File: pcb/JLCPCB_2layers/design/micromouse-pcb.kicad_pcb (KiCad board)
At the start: 4 copper layers, 100 x 120 mm, 184 parts, among them J1 BATT_IN_2S, J10 BATT_IN_XT60 (parallel option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, J5 MOTOR_A_N20_ENCODER, J6 MOTOR_B_N20_ENCODER, J7 USB-C rear (GCT USB4105; VBUS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, J8 JTAG_1x6 (3V3,TMS,TCK,TDO,TDI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, J9 BALANCE_2S, Q1 Q_PMOS reverse guard (DMP3098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, Q16 BSS138 (real part; Q_NMOS_GSD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, Q17 BSS138 (real part; Q_NMOS_GSD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, Q18 BSS138 (real part; Q_NMOS_GSD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, Q19 BSS138 (real part; Q_NMOS_GSD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, Q2 PT334-6B (5mm filtered PT; LO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, Q20 BSS138 (real part; Q_NMOS_GSD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, Q21 BSS138 (real part; Q_NMOS_GSD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, Q22 BSS138 (real part; Q_NMOS_GSD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, Q23 BSS138 (real part; Q_NMOS_GSD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, Q24 BSS138 (real part; Q_NMOS_GSD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, Q25 BSS138 (real part; Q_NMOS_GSD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, Q26 BSS138 (real part; Q_NMOS_GSD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, Q27 BSS138 (real part; Q_NMOS_GSD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, Q28 BSS84 (PMOS indicator driver;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, Q29 BSS84 (PMOS indicator driver;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, Q3 PT334-6B (5mm filtered PT; LO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, Q30 BSS84 (PMOS indicator driver;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, Q31 BSS84 (PMOS indicator driver;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, Q32 BSS84 (PMOS indicator driver;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, Q33 BSS84 (PMOS indicator driver;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, Q34 MMBT2222A (buzzer low-side dr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, Q4 PT334-6B (5mm filtered PT; LO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, Q5 PT334-6B (5mm filtered PT; LO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, Q6 PT334-6B (5mm filtered PT; LO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, Q7 PT334-6B (5mm filtered PT; LO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, SW1 BTN_A (start / BOOT), SW2 RESET, SW3 BTN_B, SW4 BTN_C, SW5 PWR ALL (PCM12SMTR slide; sli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, SW6 PWR MOTORS (PCM12SMTR slide; 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, U1 AP63203WU-7 (fixed 3.3V 2A bu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, U2 TB6612FNG, U3 ESP32-S3-WROOM-1-N8R2 (quad P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, U4 CD74HC4067M, U6 USBLC6-2SC6 (SOT-23-6; 2P6 ba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, U7 TPS54302DDCR (6.0V/3A motor b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, U8 BNO055 (9-axis IMU + fusion; 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

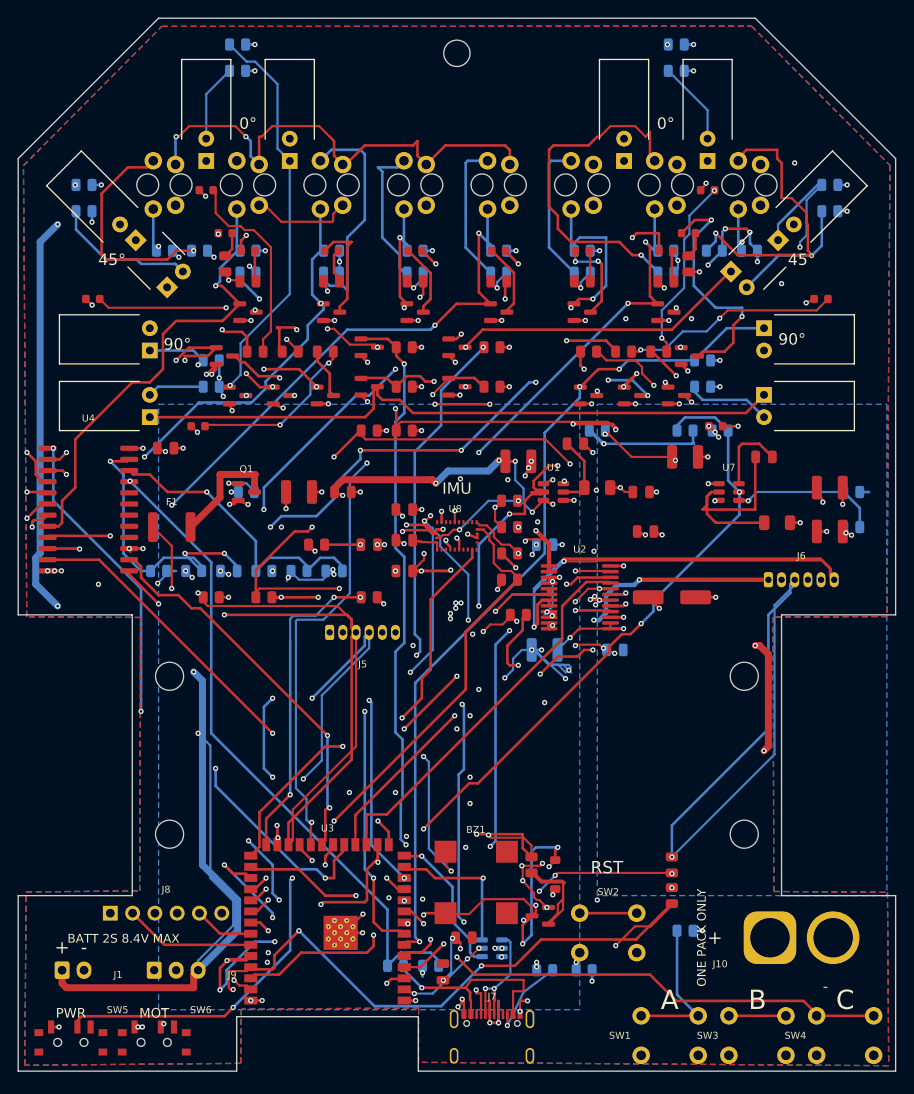
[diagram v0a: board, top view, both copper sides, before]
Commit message: 2-layer JLCPCB: initial placement + render (for review)
build_pcb.py adapted for the 2-layer part set:
- 2 copper layers (was 4); inner GND/3V3 planes replaced by solid GND pours on
  both outer layers (power rails routed as traces in the routing phase).
- Skip-missing placement wrapper drops the removed parts (line array LS1-8,
  line indicators, mux U4, JTAG J8) automatically; retained parts keep their
  4-layer positions.
- Restored the buzzer cluster (BZ1/Q34/D29/R81) + XT60 J10 placements (they were
  hand-placed in the frozen 4-layer board, never in build_pcb.py).
- Placed the new power/status/RGB LEDs (D30/D31/D32 + R82/R83/C31), provisional.
- THT hand-solder-margin gate downgraded to advisory (board is JLC machine-
  assembled); the one flagged pair (SW2<->R12, 2.04mm) will be nudged clear in
  refinement.

Board: 2 layers, 137 footprints, all 398 pins mapped, no courtyard overlaps,
bodies inside outline. Renders in images/placement_{top,bottom}.png.

Refinement next: motor connectors J5/J6 symmetric, J9 balance "OPTIONAL" silk,
confirm side indicators clear of IR beams, ALL refdes on silk, route to DRC 0/0.

Co-Authored-By: Claude Fable 5 <noreply@anthropic.com>
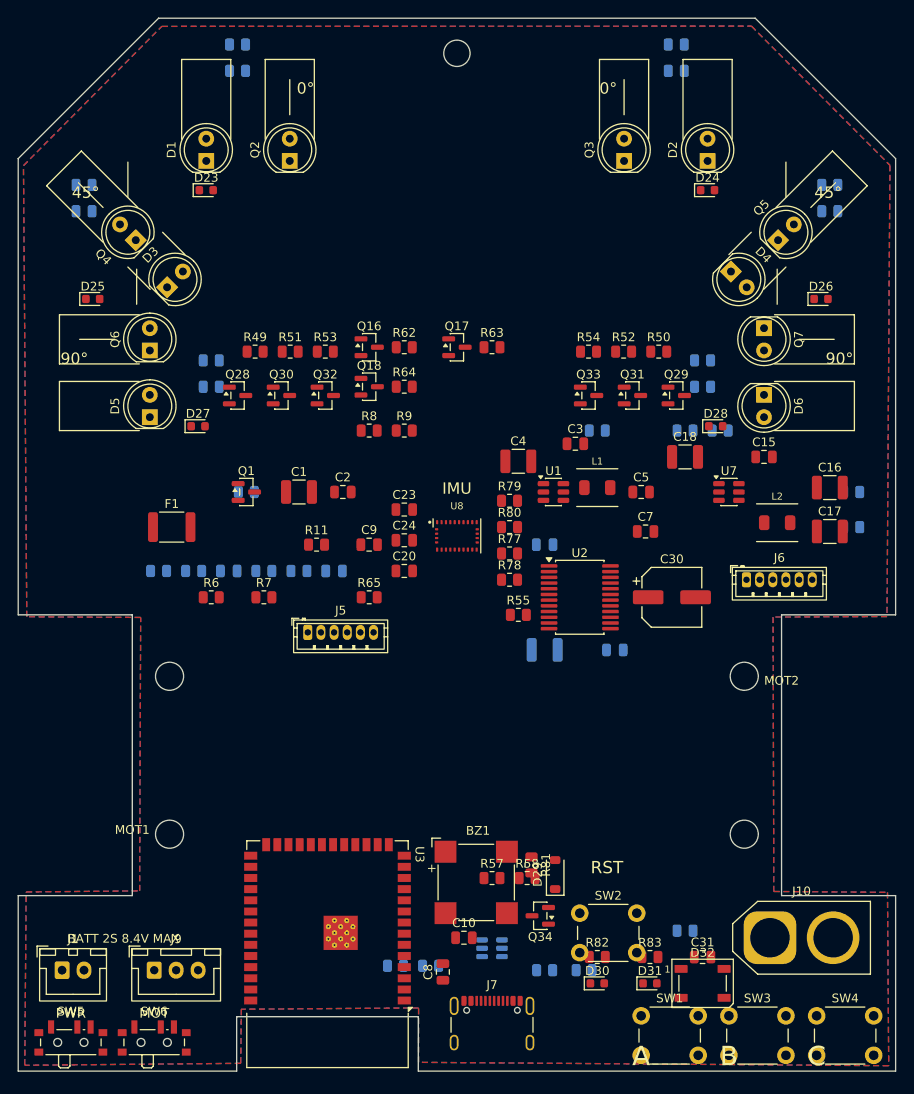
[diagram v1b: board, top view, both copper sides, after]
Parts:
- removed C13: 100nF, Capacitor_SMD:C_0805_2012Metric
- removed D15, D16, D17, D18, D19, D20, D21, D22: Indicator LED 0603 super-red AlInGaP, high-efficiency bin R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, LED_SMD:LED_0603_1608Metric
- removed J8: JTAG_1x6 (3V3,TMS,TCK,TDO,TDI,GND), Connector_PinHeader_2.54mm:PinHeader_1x06_P2.54mm_Vertical
- removed LS1, LS2, LS3, LS4, LS5, LS6, LS7, LS8: TCRT5000 (reflective sensor, filtered PT; PC817 base symbol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, n20:TCRT5000
- removed Q19, Q20, Q21, Q22, Q23, Q24, Q25, Q26, Q27: BSS138 (real part; Q_NMOS_GSD base symbol used so ERC check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, Package_TO_SOT_SMD:SOT-23
- removed R25, R27, R29, R31, R33, R35, R37, R39: 47k, Resistor_SMD:R_0805_2012Metric
- removed R26, R28, R30, R32, R34, R36, R38, R40: 120, Resistor_SMD:R_0805_2012Metric
- removed R41, R42, R43, R44, R45, R46, R47, R48: 1k, Resistor_SMD:R_0805_2012Metric
- removed R61: 100k, Resistor_SMD:R_0805_2012Metric
- removed U4: CD74HC4067M, Package_SO:SOIC-24W_7.5x15.4mm_P1.27mm
- added C31: C_0805_2012Metric, C_0805_2012Metric, F.Cu at (78.0, 107.0)
- added D30: LED_0603_1608Metric, LED_0603_1608Metric, F.Cu at (66.0, 110.0)
- added D31: LED_0603_1608Metric, LED_0603_1608Metric, F.Cu at (72.0, 110.0)
- added D32: LED_WS2812B_PLCC4_5.0x5.0mm_P3.2mm, LED_WS2812B_PLCC4_5.0x5.0mm_P3.2mm, F.Cu at (78.0, 110.0)
- added R82: R_0805_2012Metric, R_0805_2012Metric, F.Cu at (66.0, 107.0)
- added R83: R_0805_2012Metric, R_0805_2012Metric, F.Cu at (72.0, 107.0)
- BZ1: value CMT-8504-100-SMT (magnetic transducer 8.5mm, 15R coil, 4kHz; pads 3/4 are mechanical dummies) -> MagneticBuzzer_CUI_CMT-8504-100-SMT; footprint Buzzer_Beeper:MagneticBuzzer_CUI_CMT-8504-100-SMT -> MagneticBuzzer_CUI_CMT-8504-100-SMT
- C1, C11, C16, C17, C18, C4: footprint Capacitor_SMD:C_1210_3225Metric -> C_1210_3225Metric
- C10: value 10uF -> C_0805_2012Metric; footprint Capacitor_SMD:C_0805_2012Metric -> C_0805_2012Metric
- C12, C14, C15, C2, C24, C3, C5, C7: footprint Capacitor_SMD:C_0805_2012Metric -> C_0805_2012Metric
- C19, C20, C23, C6, C8: value 100nF -> C_0805_2012Metric; footprint Capacitor_SMD:C_0805_2012Metric -> C_0805_2012Metric
- C30: footprint Capacitor_SMD:CP_Elec_6.3x7.7 -> CP_Elec_6.3x7.7
- C9: value 1uF -> C_0805_2012Metric; footprint Capacitor_SMD:C_0805_2012Metric -> C_0805_2012Metric
- D1, D2, D3, D4, D5, D6: value IR333-A (Everlight 5mm 940nm 20deg; LD271 base symbol; TSAL6400 is lifecycle-Obsolete at Lion) -> LED_D5.0mm_IRGrey; footprint LED_THT:LED_D5.0mm_IRGrey -> LED_D5.0mm_IRGrey
- D23, D24, D25, D26, D27, D28: value Indicator LED 0603 super-red AlInGaP, high-eff bin (e.g. APT1608SURCK) -> LED_0603_1608Metric; footprint LED_SMD:LED_0603_1608Metric -> LED_0603_1608Metric
- D29: value 1N4148W (flyback clamp across the buzzer coil) -> D_SOD-123; footprint Diode_SMD:D_SOD-123 -> D_SOD-123
- F1: value 2.6A/16V PPTC -> Fuse_1812_4532Metric; footprint Fuse:Fuse_1812_4532Metric -> Fuse_1812_4532Metric
- J1: value BATT_IN_2S -> JST_XH_B2B-XH-A_1x02_P2.50mm_Vertical; footprint Connector_JST:JST_XH_B2B-XH-A_1x02_P2.50mm_Vertical -> JST_XH_B2B-XH-A_1x02_P2.50mm_Vertical
- J10: value BATT_IN_XT60 (parallel option -- ONE PACK ONLY) -> AMASS_XT60-M_1x02_P7.20mm_Vertical; footprint Connector_AMASS:AMASS_XT60-M_1x02_P7.20mm_Vertical -> AMASS_XT60-M_1x02_P7.20mm_Vertical
- J5: value MOTOR_A_N20_ENCODER -> JST_ZH_B6B-ZR_1x06_P1.50mm_Vertical; footprint Connector_JST:JST_ZH_B6B-ZR_1x06_P1.50mm_Vertical -> JST_ZH_B6B-ZR_1x06_P1.50mm_Vertical
- J6: value MOTOR_B_N20_ENCODER -> JST_ZH_B6B-ZR_1x06_P1.50mm_Vertical; footprint Connector_JST:JST_ZH_B6B-ZR_1x06_P1.50mm_Vertical -> JST_ZH_B6B-ZR_1x06_P1.50mm_Vertical
- J7: value USB-C rear (GCT USB4105; VBUS unused -- battery powers the board) -> USB_C_Receptacle_GCT_USB4105-xx-A_16P_TopMnt_Horizontal; footprint Connector_USB:USB_C_Receptacle_GCT_USB4105-xx-A_16P_TopMnt_Horizontal -> USB_C_Receptacle_GCT_USB4105-xx-A_16P_TopMnt_Horizontal
- J9: value BALANCE_2S -> JST_XH_B3B-XH-A_1x03_P2.50mm_Vertical; footprint Connector_JST:JST_XH_B3B-XH-A_1x03_P2.50mm_Vertical -> JST_XH_B3B-XH-A_1x03_P2.50mm_Vertical
- L1, L2: footprint n20:L_Bourns_SRP4020TA -> L_Bourns_SRP4020TA
- Q1: value Q_PMOS reverse guard (DMP3098L-7: Vgs +/-20V, 2S-safe) -> SOT-23; footprint Package_TO_SOT_SMD:SOT-23 -> SOT-23
- Q16, Q17, Q18: value BSS138 (real part; Q_NMOS_GSD base symbol used so ERC checks pins) -> SOT-23; footprint Package_TO_SOT_SMD:SOT-23 -> SOT-23
- Q2, Q3, Q4, Q5, Q6, Q7: value PT334-6B (5mm filtered PT; LONG LEAD = EMITTER; SFH309 base symbol so ERC checks pins) -> LED_D5.0mm_IRBlack; footprint LED_THT:LED_D5.0mm_IRBlack -> LED_D5.0mm_IRBlack
- Q28, Q29, Q30, Q31, Q32, Q33: value BSS84 (PMOS indicator driver; Q_PMOS base symbol) -> SOT-23; footprint Package_TO_SOT_SMD:SOT-23 -> SOT-23
- Q34: value MMBT2222A (buzzer low-side driver; Q_NPN_BEC base symbol so ERC checks pins) -> SOT-23; footprint Package_TO_SOT_SMD:SOT-23 -> SOT-23
- R1, R2, R62, R63, R64, R69, R73, R75, R76: value 100k -> R_0805_2012Metric; footprint Resistor_SMD:R_0805_2012Metric -> R_0805_2012Metric
- R10, R11, R55, R6, R65, R67, R7, R79, R8, R80, R9: value 10k -> R_0805_2012Metric; footprint Resistor_SMD:R_0805_2012Metric -> R_0805_2012Metric
- R12, R56: value 5.1k -> R_0805_2012Metric; footprint Resistor_SMD:R_0805_2012Metric -> R_0805_2012Metric
- R13, R15, R17, R19, R21, R23: value 47k -> R_0805_2012Metric; footprint Resistor_SMD:R_0805_2012Metric -> R_0805_2012Metric
- R14, R16, R18, R20, R22, R24: value 33 -> R_0805_2012Metric; footprint Resistor_SMD:R_0805_2012Metric -> R_0805_2012Metric
- R3: value 39k -> R_0805_2012Metric; footprint Resistor_SMD:R_0805_2012Metric -> R_0805_2012Metric
- R49, R50, R51, R52, R53, R54, R57, R58: value 1k -> R_0805_2012Metric; footprint Resistor_SMD:R_0805_2012Metric -> R_0805_2012Metric
- R68: value 15k -> R_0805_2012Metric; footprint Resistor_SMD:R_0805_2012Metric -> R_0805_2012Metric
- R70: value 220k -> R_0805_2012Metric; footprint Resistor_SMD:R_0805_2012Metric -> R_0805_2012Metric
- R71: value 110k -> R_0805_2012Metric; footprint Resistor_SMD:R_0805_2012Metric -> R_0805_2012Metric
- R74: value 11k -> R_0805_2012Metric; footprint Resistor_SMD:R_0805_2012Metric -> R_0805_2012Metric
- R77, R78: value 4.7k -> R_0805_2012Metric; footprint Resistor_SMD:R_0805_2012Metric -> R_0805_2012Metric
- R81: value 220 -> R_0805_2012Metric; footprint Resistor_SMD:R_0805_2012Metric -> R_0805_2012Metric
- SW1: value BTN_A (start / BOOT) -> SW_PUSH_6mm; footprint Button_Switch_THT:SW_PUSH_6mm -> SW_PUSH_6mm
- SW2: value RESET -> SW_PUSH_6mm; footprint Button_Switch_THT:SW_PUSH_6mm -> SW_PUSH_6mm
- SW3: value BTN_B -> SW_PUSH_6mm; footprint Button_Switch_THT:SW_PUSH_6mm -> SW_PUSH_6mm
- SW4: value BTN_C -> SW_PUSH_6mm; footprint Button_Switch_THT:SW_PUSH_6mm -> SW_PUSH_6mm
- SW5: value PWR ALL (PCM12SMTR slide; slide-to-GND = OFF) -> SW_SPDT_PCM12; footprint Button_Switch_SMD:SW_SPDT_PCM12 -> SW_SPDT_PCM12
- SW6: value PWR MOTORS (PCM12SMTR slide; slide-to-GND = motors OFF) -> SW_SPDT_PCM12; footprint Button_Switch_SMD:SW_SPDT_PCM12 -> SW_SPDT_PCM12
- U1: value AP63203WU-7 (fixed 3.3V 2A buck; AP63200WU base symbol so ERC checks pins) -> TSOT-23-6; footprint Package_TO_SOT_SMD:TSOT-23-6 -> TSOT-23-6
- U2: value TB6612FNG -> SSOP-24_5.3x8.2mm_P0.65mm; footprint Package_SO:SSOP-24_5.3x8.2mm_P0.65mm -> SSOP-24_5.3x8.2mm_P0.65mm
- U3: value ESP32-S3-WROOM-1-N8R2 (quad PSRAM: IO35-37 usable; octal -R8 would lose them) -> ESP32-S3-WROOM-1; footprint RF_Module:ESP32-S3-WROOM-1 -> ESP32-S3-WROOM-1
- U6: value USBLC6-2SC6 (SOT-23-6; 2P6 base symbol so ERC checks pins) -> SOT-23-6; footprint Package_TO_SOT_SMD:SOT-23-6 -> SOT-23-6
- U7: value TPS54302DDCR (6.0V/3A motor buck; FB=100k/11k) -> SOT-23-6; footprint Package_TO_SOT_SMD:SOT-23-6 -> SOT-23-6
- U8: value BNO055 (9-axis IMU + fusion; 3.3V native; I2C 0x28) -> VAL; footprint n20:BNO055 -> BNO055
- moved R57 20.6 mm to (54.0, 98.0), turned to 0 degrees
- moved R58 16.6 mm to (58.0, 98.0), turned to 0 degrees
- moved J5 2.50 mm to (33.0, 70.0)
- moved J6 2.50 mm to (83.0, 64.0)
- moved J7 1.50 mm to (54.0, 115.7)
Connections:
- U3 pad 12: MUX_S3 -> BAT_MID_SENSE
- U3 pad 17: AIN1 -> VBUS_SENSE
- U3 pad 19: MUX_S0 -> AIN1
- U3 pad 20: MUX_S1 -> STATUS_LED
- U3 pad 21: MUX_S2 -> unconnected-(U3-IO13-Pad21)
- U3 pad 22: LINE_EMIT -> RGB_DATA
- U3 pad 32: JTAG_TCK -> unconnected-(U3-IO39-Pad32)
- U3 pad 33: JTAG_TDO -> unconnected-(U3-IO40-Pad33)
- U3 pad 34: JTAG_TDI -> unconnected-(U3-IO41-Pad34)
- U3 pad 35: JTAG_TMS -> unconnected-(U3-IO42-Pad35)
- U3 pad 7: MUX_SENSE -> VBAT_SENSE
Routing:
- net BATT_RAW: track 364.0 -> 0.00 mm, vias 8 -> 0
- net ENC2_A_S3: track 290.2 -> 0.00 mm, vias 15 -> 0
- net PLUS3V3: track 245.9 -> 0.00 mm, vias 79 -> 0
- net GND: track 235.8 -> 0.00 mm, vias 112 -> 0
- net ENC2_A: track 215.1 -> 0.00 mm, vias 7 -> 0
- net ENC2_B: track 200.2 -> 0.00 mm, vias 6 -> 0
- net WALL4_SENSE: track 157.1 -> 0.00 mm, vias 4 -> 0
- net WALL2_SENSE: track 139.5 -> 0.00 mm, vias 5 -> 0
- net PWR_EN: track 128.4 -> 0.00 mm, vias 6 -> 0
- net EMIT_LINE_K: track 128.4 -> 0.00 mm, vias 3 -> 0
- net ENC2_B_S3: track 120.1 -> 0.00 mm, vias 4 -> 0
- net WALL1_SENSE: track 117.0 -> 0.00 mm, vias 2 -> 0
- net MOT_EN: track 110.4 -> 0.00 mm, vias 5 -> 0
- net ESP_EN: track 107.2 -> 0.00 mm, vias 4 -> 0
- net ENC1_B: track 103.9 -> 0.00 mm, vias 8 -> 0
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- removed copper zone on In1.Cu, net GND
- removed copper zone on In2.Cu, net PLUS3V3
- removed copper zone on B.Cu, net VM_6V
- removed copper zone on B.Cu, net VM_BATT
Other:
- copper layers 4 -> 2
- board text removed: "+"
- board text removed: "-"
- board text removed: "ONE PACK ONLY"

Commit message: 2-layer placement refinement (user render feedback)
- Removed the U-shaped body-silk "boxes" around the wall-sensor LEDs; kept the
  0/45/90-deg angle callouts.
- Motor connectors J5/J6 now SYMMETRIC (both x=33/67, y=70) -- moved the motor
  driver U2 (+ C11/C12/C30) to the motor-bay center so J6's mirror spot is free.
- Moved the 3 user buttons (SW1/SW3/SW4 = BTN_A/B/C) and the RGB (D32+C31) to
  the open front-center, clear of all sensor beams; RST (SW2) + power/status
  LEDs stay at the rear.
- No courtyard overlaps; all 398 pins mapped; bodies inside outline.

Still to do: J9 "OPTIONAL" silk, confirm side indicators clear of IR, ALL
refdes on silk, then route to DRC 0/0.

Co-Authored-By: Claude Fable 5 <noreply@anthropic.com>
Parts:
- moved D32 94.3 mm to (50.0, 20.0)
- moved C31 93.4 mm to (44.0, 20.0)
- moved SW1 91.1 mm to (40.0, 28.0)
- moved SW3 91.1 mm to (50.0, 28.0)
- moved SW4 91.1 mm to (60.0, 28.0)
- moved C30 22.5 mm to (61.0, 84.0)
- moved U2 18.4 mm to (50.0, 78.0)
- moved J6 17.1 mm to (67.0, 70.0)
- moved C11 15.2 mm to (46.0, 78.0)
- moved C12 15.2 mm to (54.0, 78.0)

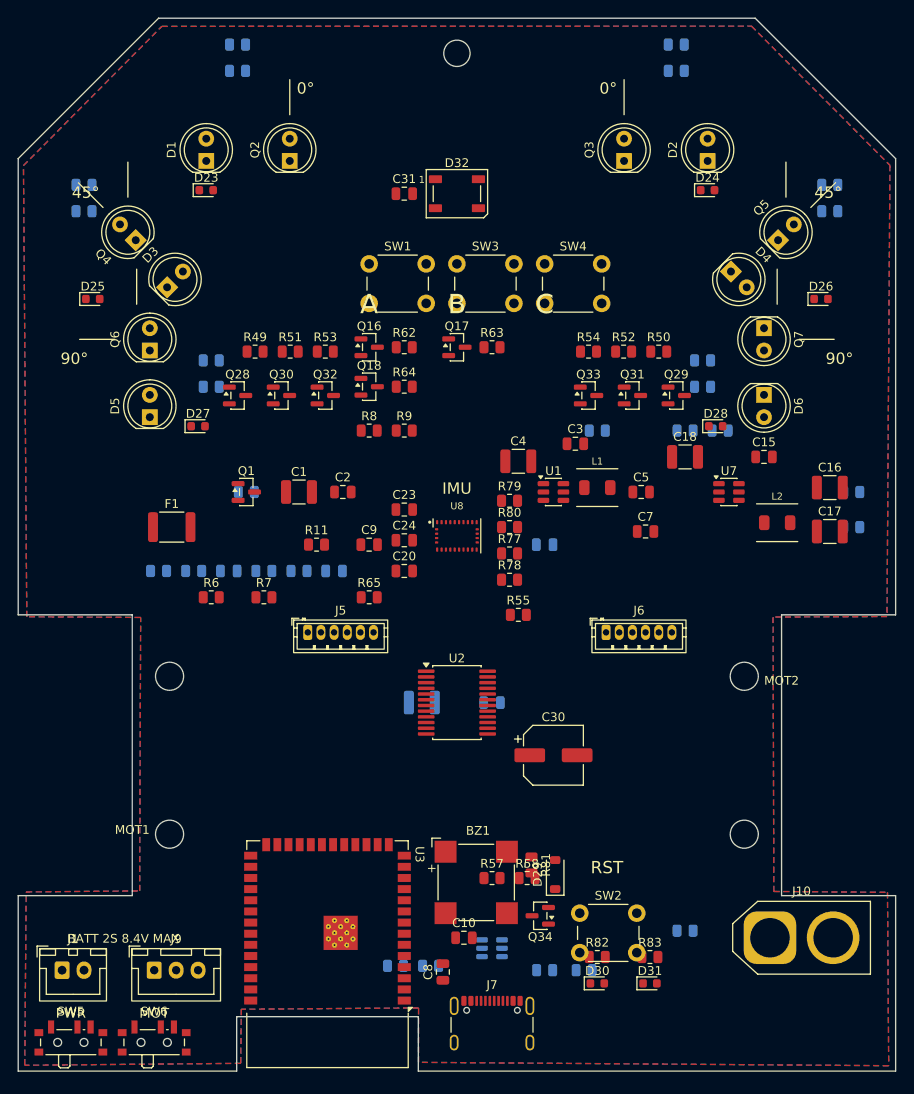
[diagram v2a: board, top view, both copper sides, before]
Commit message: 2-layer: add motor-power LED (D33), shift ESP off the left wheel
- New motor-rail indicator LED D33 (+R84): ON when SW6 is on and VM_6V is up
  (VM_6V -> 1k -> LED -> GND). Grouped with D30 (power) / D31 (status) at the
  rear by RST as three labeled indicators.
- ESP U3 shifted +2.75mm toward centre (35.25 -> 38.0) with its antenna notch
  (board_geom ANT_NOTCH) + ribbon keepout: left-wheel clearance 0.75mm -> ~3.5mm
  (max shift the rear-centre buzzer allows without relocating it).
- ESP decoupling C8/C10 moved to the bottom face under U3 (buzzer blocks the
  top-face gap). No courtyard overlaps; ERC 0; 138 components.

Renders updated. Full dead-centre ESP would need relocating the buzzer cluster
(rear-centre is packed) -- offered to the user.

Co-Authored-By: Claude Fable 5 <noreply@anthropic.com>
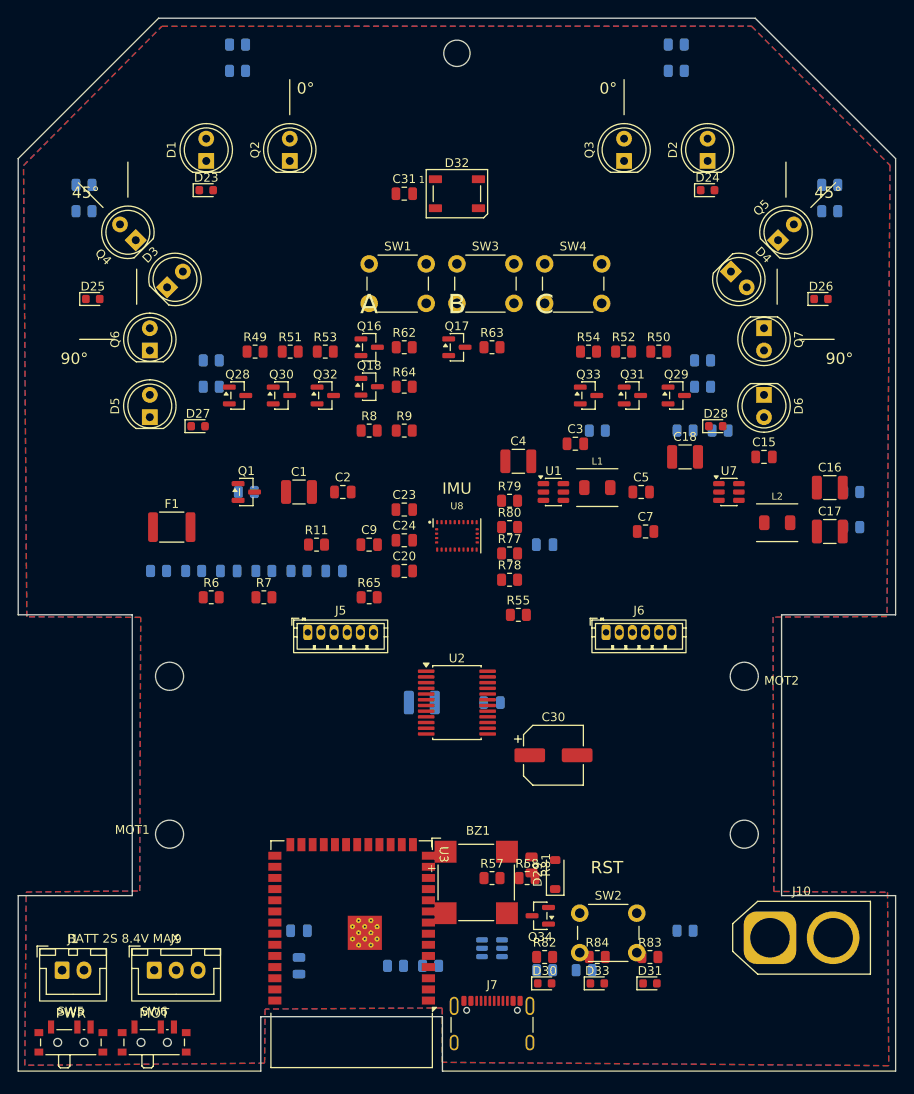
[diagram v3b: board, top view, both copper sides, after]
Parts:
- added D33: LED_0603_1608Metric, LED_0603_1608Metric, F.Cu at (66.0, 110.0)
- added R84: R_0805_2012Metric, R_0805_2012Metric, F.Cu at (66.0, 107.0)
- C10, C8: moved to B.Cu
- moved C10 18.8 mm to (32.0, 104.0), turned to 180 degrees
- moved C8 16.4 mm to (32.0, 108.0)
- moved D30 6.00 mm to (60.0, 110.0)
- moved R82 6.00 mm to (60.0, 107.0)
- moved U3 2.75 mm to (38.0, 106.7)
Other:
- outline, holes or cut-outs redrawn

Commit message: 2-layer: centre the ESP, declutter rear, name LEDs/switches, fix C30-in-motor
Coordinated rear + motor re-placement (user render feedback):
- ESP U3 CENTRED (x50) with the antenna notch dead-centre -- clears both wheels
  by ~8mm. Bottom-face parts (U6/R67/R68/C8/C10) ride under it.
- Rear declutter: USB-C J7 -> rear-right; the 3 indicator LEDs (D30/D33/D31)
  -> rear-left by the battery/switches; buzzer cluster (BZ1/Q34/D29/R81) -> the
  freed forward-left; R57/R58 flank the module.
- C30 (220uF) was overlapping the RIGHT MOTOR keepout -> moved to the motor-bay
  corridor behind U2 (out of the motor). C11/C12 stacked in the corridor.
- J6 TRUE-mirrored (rot 180) so its body mirrors J5, not just the placement
  point (the connector footprint extends one way).
- Silk: function names on all LEDs (PWR/MOT/STAT/RGB) + J9 "BAL (OPT)".

No courtyard overlaps; ERC 0; 138 components. Note: a full 5mm forward move of
J5/J6 is blocked by the dense mid-row passives (held at y70).

Co-Authored-By: Claude Fable 5 <noreply@anthropic.com>
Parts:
- moved R81 66.7 mm to (15.0, 46.0)
- moved D29 63.4 mm to (29.0, 43.0)
- moved Q34 62.3 mm to (29.0, 48.0)
- moved BZ1 60.6 mm to (22.0, 46.0)
- moved R82 34.0 mm to (26.0, 106.0)
- moved R83 34.0 mm to (38.0, 106.0)
- moved R84 34.0 mm to (32.0, 106.0)
- moved D30 34.0 mm to (26.0, 110.0)
- moved D31 34.0 mm to (38.0, 110.0)
- moved D33 34.0 mm to (32.0, 110.0)
- moved C10 22.0 mm to (54.0, 103.0)
- moved J7 16.0 mm to (70.0, 115.7)
- moved C8 14.9 mm to (46.0, 103.0)
- moved U3 12.0 mm to (50.0, 106.7)
- moved U6 11.7 mm to (64.0, 112.0)
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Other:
- outline, holes or cut-outs redrawn
- board text added: "BAL (OPT)"
- board text added: "STAT"
